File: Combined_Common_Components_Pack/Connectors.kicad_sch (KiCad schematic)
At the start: 20 parts, among them J1 BR8MC1-4, J2 BR8MC1-3, J3 BR8MC1-10, J7 USB_C_Receptacle_USB2.0_8P

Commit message: Added some connectors and basic parts
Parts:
- removed J1: BR8MC1-4, Library_GF:PhoenixContact_MCV_1,5_4-G-5.08_1x04_P5.08mm_Vertical, symbol Connector_Generic:Conn_01x04
- removed J2: BR8MC1-3, Library_GF:PhoenixContact_MCV_1,5_3-G-5.08_1x03_P5.08mm_Vertical, symbol Connector_Generic:Conn_01x03
- removed J3: BR8MC1-10, Library_GF:PhoenixContact_MCV_1,5_10-G-5.08_1x10_P5.08mm_Vertical, symbol Connector_Generic:Conn_01x10
- added J1: 5.08-10P-90, Connector_Phoenix_MSTB:PhoenixContact_MSTBA_2,5_10-G-5,08_1x10_P5.08mm_Horizontal, symbol Connector_Generic:Conn_01x10
- added J10: 5.08-03P-180, Connector_Phoenix_MSTB:PhoenixContact_MSTBVA_2,5_3-G-5,08_1x03_P5.08mm_Vertical, symbol Connector_Generic:Conn_01x03
- added J11: 5.08-10P-180, Connector_Phoenix_MSTB:PhoenixContact_MSTBVA_2,5_10-G-5,08_1x10_P5.08mm_Vertical, symbol Connector_Generic:Conn_01x10
- added J12: 5.08-4P-180, Connector_Phoenix_MSTB:PhoenixContact_MSTBVA_2,5_4-G-5,08_1x04_P5.08mm_Vertical, symbol Connector_Generic:Conn_01x04
- added J13: IDC-20P-180, Connector_IDC:IDC-Header_2x10_P2.54mm_Vertical, symbol Connector_Generic:Conn_02x10_Odd_Even
- added J14: IDC-20P-90, Connector_IDC:IDC-Header_2x10_P2.54mm_Horizontal, symbol Connector_Generic:Conn_02x10_Odd_Even
- added J15: 5.08-2P-90, Connector_Phoenix_MSTB:PhoenixContact_MSTBA_2,5_2-G-5,08_1x02_P5.08mm_Horizontal, symbol Connector_Generic:Conn_01x02
- added J2: 5.08-4P-90, Connector_Phoenix_MSTB:PhoenixContact_MSTBA_2,5_4-G-5,08_1x04_P5.08mm_Horizontal, symbol Connector_Generic:Conn_01x04
- added J3: 3.81-3P, Connector_Phoenix_MC:PhoenixContact_MC_1,5_3-G-3.81_1x03_P3.81mm_Horizontal, symbol Connector_Generic:Conn_01x03
- added J9: 3.81-2P, Connector_Phoenix_MC:PhoenixContact_MC_1,5_2-G-3.81_1x02_P3.81mm_Horizontal, symbol Connector_Generic:Conn_01x02
- Batt1: Observations 90º XH-2.54mm -> 2P-XH2.54-90
- Batt2: Observations 180º JST1.25mm 2P -> 2P-1.25mm
- PORT1: value 180º JST1.25mm 4P -> 4P-1.25mm
- SERIAL2: value 180º JST1.25mm 6P -> 6P-1.25mm
- SPK2: Observations 180º XH2.54 -> 2P-XH2.54-180
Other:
- note added: "180º"
- note added: "3.81mm"
- note added: "5.08mm"
- note added: "90º"
- note added: "90º 180º"
- note added: "JST 1.25mm 180º"
- note added: "JST 1.25mm 90º"
- moved on the sheet: Batt1, PORT1, SERIAL2, SPK2, VDC1

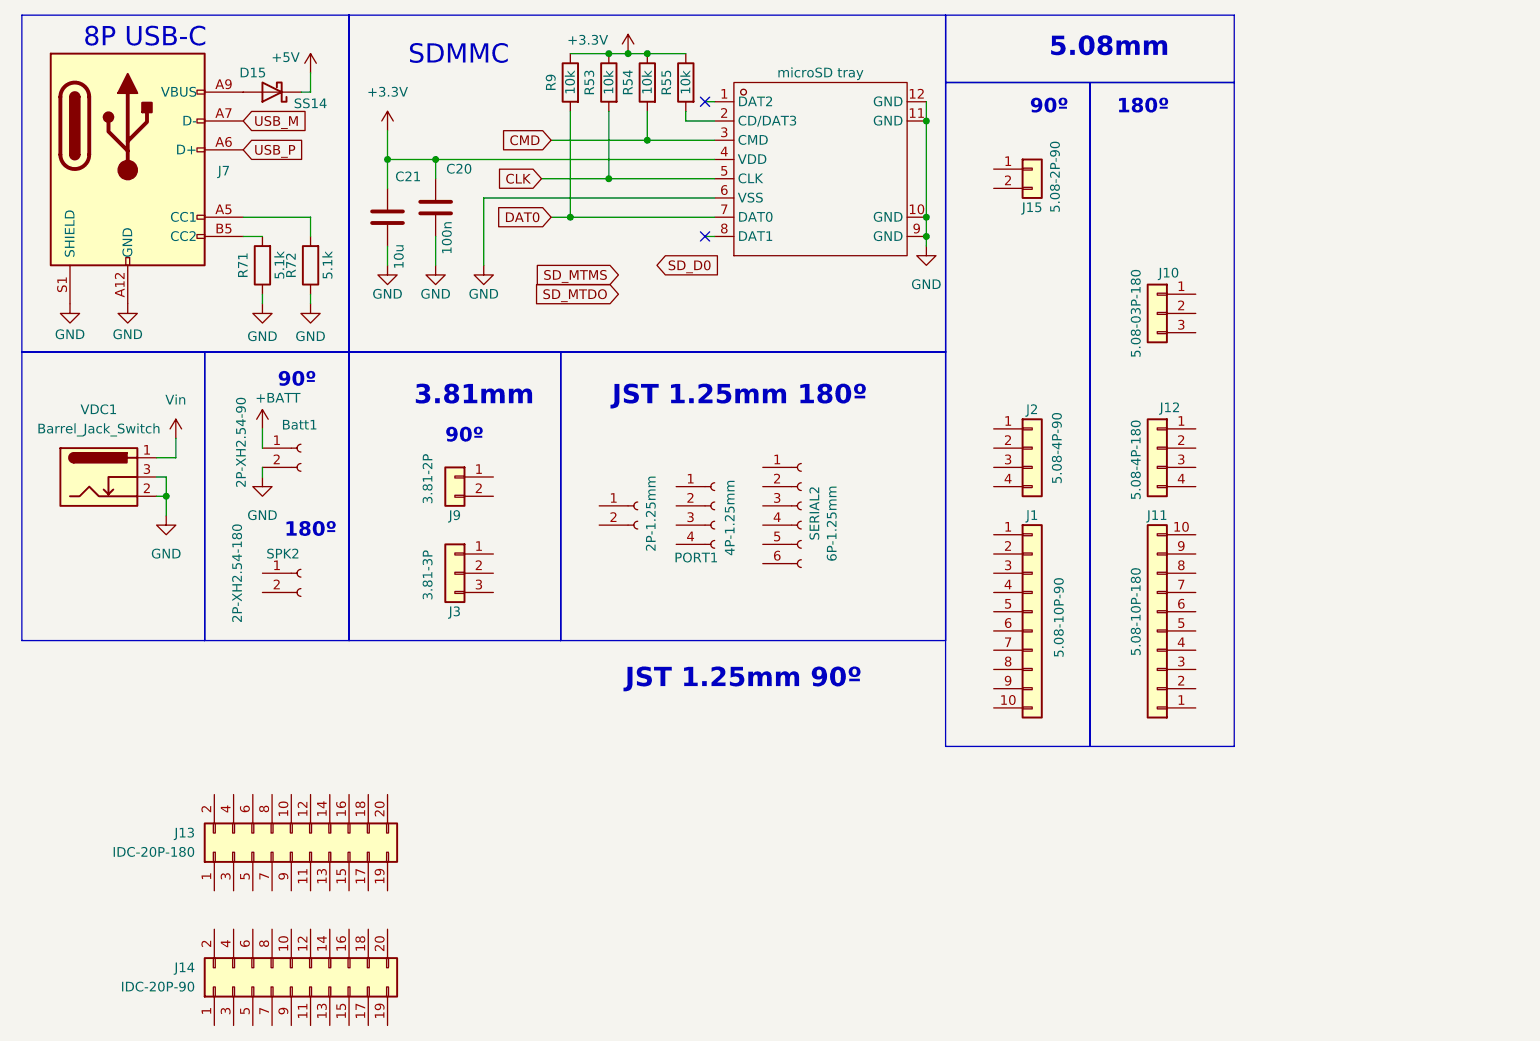
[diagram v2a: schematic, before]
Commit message: Minor updates
Basically components annotation, and more basic parts added
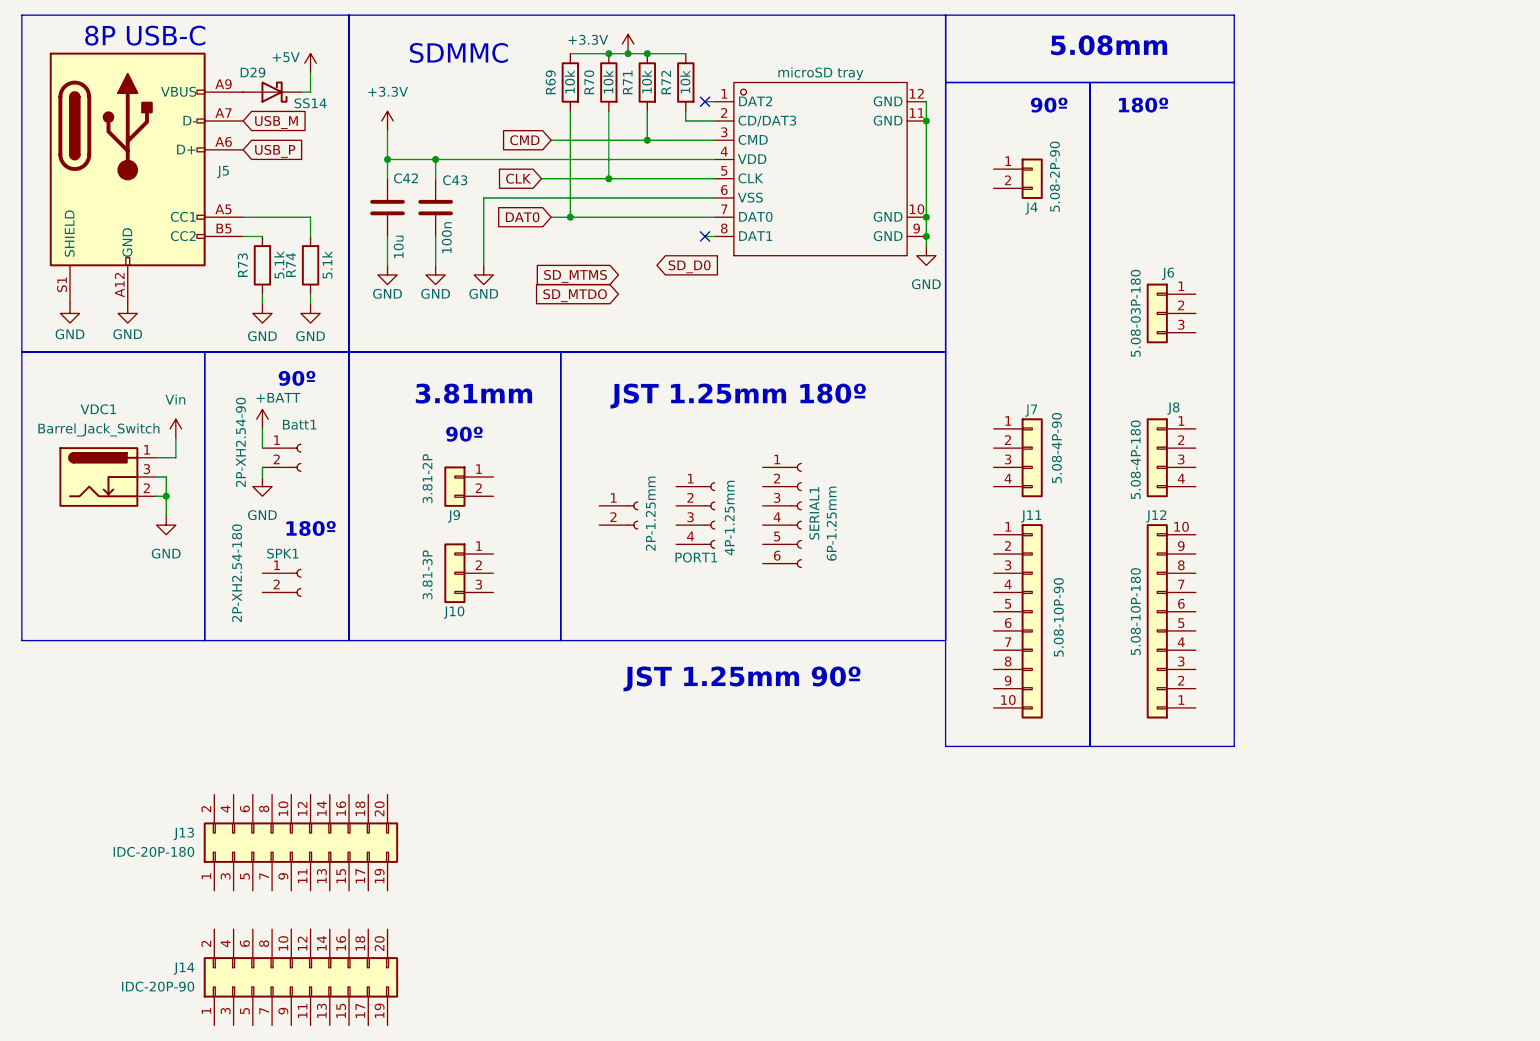
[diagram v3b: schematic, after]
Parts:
- renumbered C21 to C42, C20 to C43, D15 to D29, J3 to J10, J1 to J11, J11 to J12, J15 to J4, J7 to J5, J10 to J6, J2 to J7, J12 to J8, R9 to R69, R53 to R70, R54 to R71, R55 to R72, R71 to R73, R72 to R74, SERIAL2 to SERIAL1, SPK2 to SPK1
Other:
- moved on the sheet: C42

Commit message: Minor updates
Started footprint library for easier cross-computer design management.
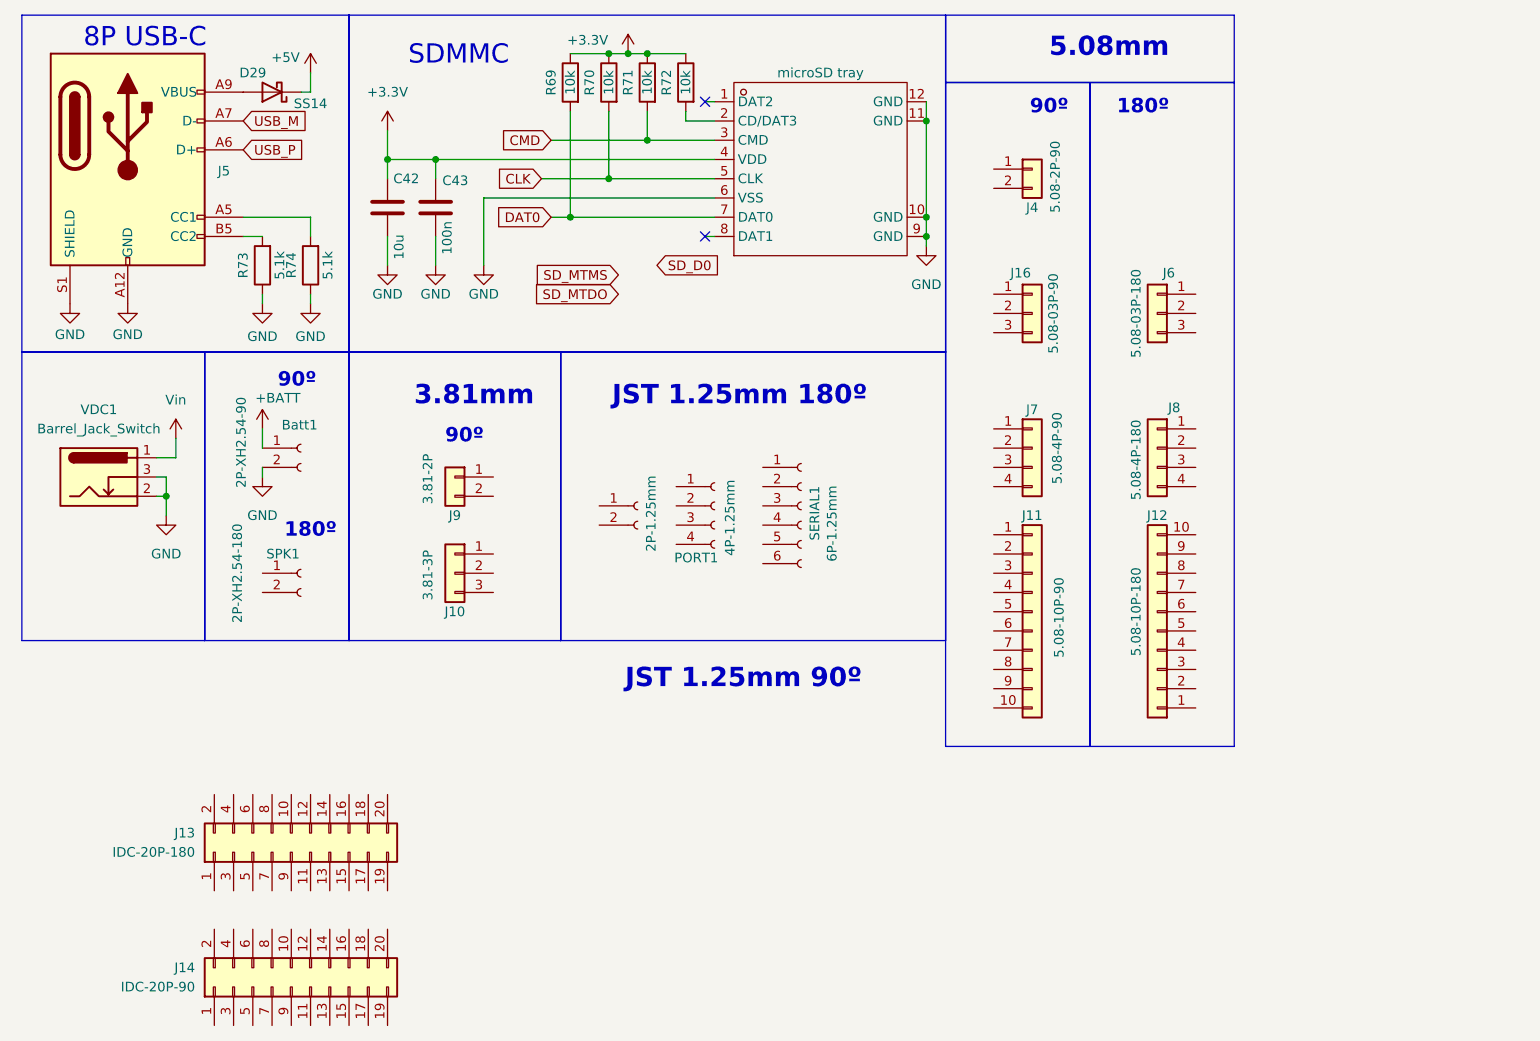
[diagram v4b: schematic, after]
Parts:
- added J16: 5.08-03P-90, Connector_Phoenix_MC_HighVoltage:PhoenixContact_MC_1,5_3-G-5.08_1x03_P5.08mm_Horizontal, symbol Connector_Generic:Conn_01x03
